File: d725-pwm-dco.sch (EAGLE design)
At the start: 62 parts, among them U1 SCREW-M2X8, U10 FX2-20S-1.27DS, U11 ERM1-5MM, U2 SCREW-M2X8, U3 NUT-M2-SELFLOCK, U4 NUT-M2-SELFLOCK, U5 FX2-20P-1.27DS, U6 SCREW-M2X8, U7 SCREW-M2X8, U8 NUT-M2-SELFLOCK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

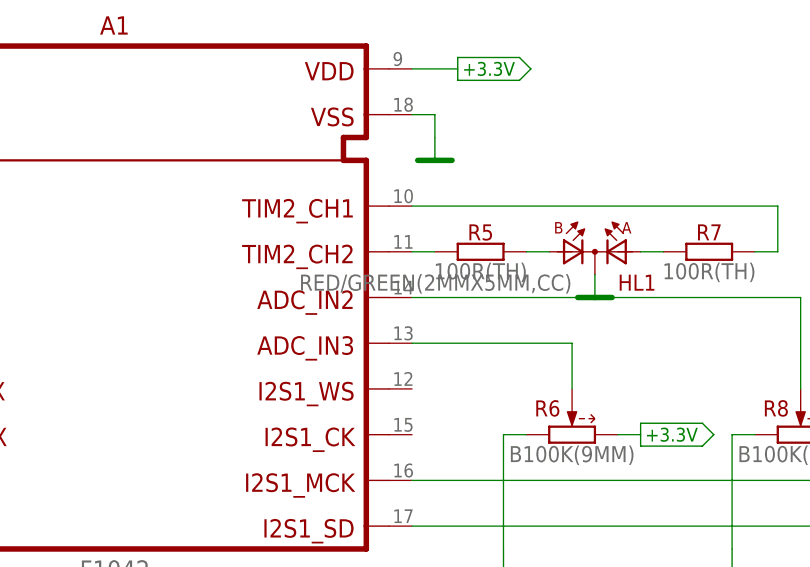
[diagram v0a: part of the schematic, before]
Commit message: D725 LED Color Change
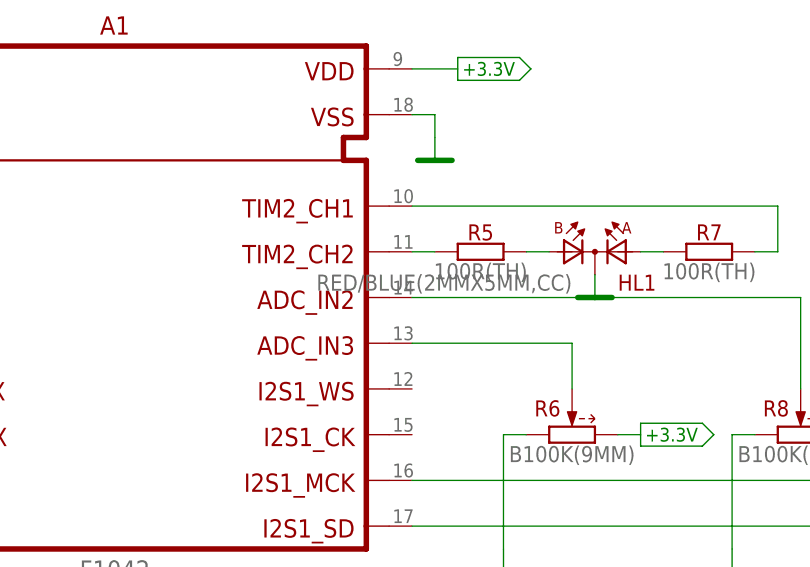
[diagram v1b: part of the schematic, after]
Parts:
- HL1: value RED/GREEN(2MMX5MM,CC) -> RED/BLUE(2MMX5MM,CC); device optoelectronics:RED/GREEN(2MMX5MM,CC) -> optoelectronics:RED/BLUE(2MMX5MM,CC)
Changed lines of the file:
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@@
 <part name="R5" library="resistors" deviceset="?" device="100R(TH)"/>
 <part name="R7" library="resistors" deviceset="?" device="100R(TH)"/>
-<part name="HL1" library="optoelectronics" deviceset="?(2MMX5MM,CC)" device="RED/GREEN"/>
+<part name="HL1" library="optoelectronics" deviceset="?(2MMX5MM,CC)" device="RED/BLUE" value="RED/BLUE(2MMX5MM,CC)"/>
 <part name="GND8" library="supply" deviceset="GND" device=""/>
 <part name="GND2" library="supply" deviceset="GND" device=""/>
